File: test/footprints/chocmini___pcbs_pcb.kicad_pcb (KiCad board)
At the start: 2 copper layers, 11.6 x 6.6 mm, 3 parts

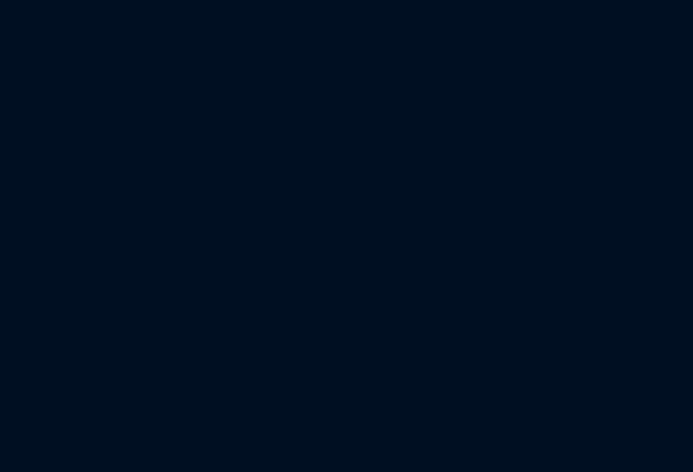
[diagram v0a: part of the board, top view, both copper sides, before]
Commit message: expand code coverage for `chocmini` footprint
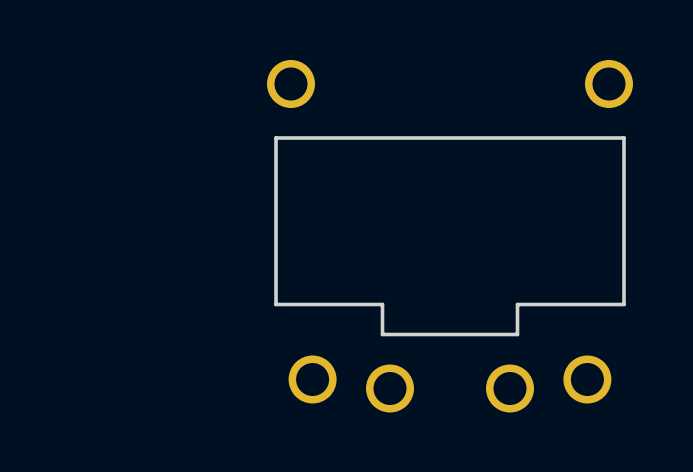
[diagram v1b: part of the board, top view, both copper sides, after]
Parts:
- added S4: Kailh_PG1232, lib:Kailh_PG1232, F.Cu at (150.0, 0.00)
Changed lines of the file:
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@@
+        (pad 2 thru_hole circle (at -2 5.4) (size 1.6 1.6) (drill 1.1) (layers *.Cu *.Mask) (net 2 "to") (clearance 0.2))
+			  )
+        (module lib:Kailh_PG1232 (layer F.Cu)
+        (at 150 0 0)
+        (fp_text reference "S4" (at 0 0) (layer F.SilkS) hide (effects (font (size 1.27 1.27) (thickness 0.15))))
+        (fp_text value Kailh_PG1232 (at 0 -7.3) (layer F.Fab) (effects (font (size 1 1) (thickness 0.15))))
+        (fp_line (start -7.25 -6.75) (end -6.25 -6.75) (layer Dwgs.User) (width 0.15))
+        (fp_line (start -7.25 -6.75) (end -7.25 -5.75) (layer Dwgs.User) (width 0.15))
+        (fp_line (start -7.25 6.75) (end -6.25 6.75) (layer Dwgs.User) (width 0.15))
+        (fp_line (start -7.25 6.75) (end -7.25 5.75) (layer Dwgs.User) (width 0.15))
+        (fp_line (start 7.25 -6.75) (end 6.25 -6.75) (layer Dwgs.User) (width 0.15))
+        (fp_line (start 7.25 -6.75) (end 7.25 -5.75) (layer Dwgs.User) (width 0.15))
+        (fp_line (start 7.25 6.75) (end 6.25 6.75) (layer Dwgs.User) (width 0.15))
+        (fp_line (start 7.25 6.75) (end 7.25 5.75) (layer Dwgs.User) (width 0.15))
+        (fp_line (start 2.8 -5.35) (end -2.8 -5.35) (layer Dwgs.User) (width 0.15))
+        (fp_line (start -2.8 -3.2) (end 2.8 -3.2) (layer Dwgs.User) (width 0.15))
+        (fp_line (start 2.8 -3.2) (end 2.8 -5.35) (layer Dwgs.User) (width 0.15))
+        (fp_line (start -2.8 -3.2) (end -2.8 -5.35) (layer Dwgs.User) (width 0.15))
+        (fp_line (start 2.25 2.6) (end 5.8 2.6) (layer Edge.Cuts) (width 0.12))
+        (fp_line (start -2.25 2.6) (end -5.8 2.6) (layer Edge.Cuts) (width 0.12))
+        (fp_line (start 2.25 3.6) (end 2.25 2.6) (layer Edge.Cuts) (width 0.12))
+        (fp_line (start -2.25 3.6) (end 2.25 3.6) (layer Edge.Cuts) (width 0.12))
+        (fp_line (start -2.25 2.6) (end -2.25 3.6) (layer Edge.Cuts) (width 0.12))
+        (fp_line (start -5.8 2.6) (end -5.8 -2.95) (layer Edge.Cuts) (width 0.12))
+        (fp_line (start 5.8 -2.95) (end 5.8 2.6) (layer Edge.Cuts) (width 0.12))
+        (fp_line (start -5.8 -2.95) (end 5.8 -2.95) (layer Edge.Cuts) (width 0.12))
+        (pad 3 thru_hole circle (at 5.3 -4.75) (size 1.6 1.6) (drill 1.1) (layers *.Cu *.Mask) (clearance 0.2))
+        (pad 4 thru_hole circle (at -5.3 -4.75) (size 1.6 1.6) (drill 1.1) (layers *.Cu *.Mask) (clearance 0.2))
+        (fp_line (start -9 -8.5) (end 9 -8.5) (layer Dwgs.User) (width 0.15))
+        (fp_line (start 9 -8.5) (end 9 8.5) (layer Dwgs.User) (width 0.15))
+        (fp_line (start 9 8.5) (end -9 8.5) (layer Dwgs.User) (width 0.15))
+        (fp_line (start -9 8.5) (end -9 -8.5) (layer Dwgs.User) (width 0.15))
+        (pad 1 thru_hole circle (at -4.58 5.1) (size 1.6 1.6) (drill 1.1) (layers *.Cu *.Mask) (net 1 "from") (clearance 0.2))
+        (pad 2 thru_hole circle (at 2 5.4) (size 1.6 1.6) (drill 1.1) (layers *.Cu *.Mask) (net 2 "to") (clearance 0.2))
+        (pad 1 thru_hole circle (at 4.58 5.1) (size 1.6 1.6) (drill 1.1) (layers *.Cu *.Mask) (net 1 "from") (clearance 0.2))
         (pad 2 thru_hole circle (at -2 5.4) (size 1.6 1.6) (drill 1.1) (layers *.Cu *.Mask) (net 2 "to") (clearance 0.2))
 			  )
